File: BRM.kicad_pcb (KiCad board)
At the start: 4 copper layers, 48 parts, among them J1 2606-1102, J2 2601-1108, J4 2601-1108, U1 TPS55289RYQR

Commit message: VRM work
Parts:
- moved R1 123.5 mm to (98.2, 65.5), turned to 180 degrees
- moved D1 118.1 mm to (99.5, 67.5)
- moved D10 60.2 mm to (163.9, 133.6)
- moved Cvcc1 52.5 mm to (151.2, 45.0)
- moved Rt1 48.5 mm to (143.0, 43.5), turned to 90 degrees
- moved Coutx2 44.5 mm to (143.5, 54.0), turned to 180 degrees
- moved Coutx1 39.3 mm to (140.5, 59.0), turned to 180 degrees
- moved Rcomp1 35.1 mm to (147.8, 50.1), turned to 90 degrees
- moved J2 24.0 mm to (155.0, 75.5)
- moved L1 23.3 mm to (140.0, 68.5)
- moved Ccomp2 21.1 mm to (147.4, 52.5)
- moved Ccomp1 20.1 mm to (147.4, 51.5)
- moved F5 19.6 mm to (155.0, 57.4)
- moved Cboot1 19.4 mm to (138.0, 56.0)
- moved F6 18.9 mm to (162.0, 49.3)
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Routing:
- net Net-(U1-SW1): track 0.00 -> 73.2 mm
- net Net-(U1-SW2): track 0.00 -> 52.9 mm
- net /VRM/Vout: track 0.00 -> 29.8 mm, vias 0 -> 8
- net Net-(D5-A): track 87.1 -> 58.1 mm
- net Net-(D3-A): track 89.2 -> 60.2 mm
- net Net-(D9-A): track 0.00 -> 29.0 mm
- net Net-(D7-A): track 0.00 -> 29.0 mm
- net Net-(D8-A): track 0.00 -> 20.9 mm
- net Net-(D2-A): track 62.6 -> 41.7 mm
- net Net-(D4-A): track 62.6 -> 41.7 mm
- net Net-(D6-A): track 0.00 -> 20.9 mm
- net Net-(U1-BOOT1): track 0.00 -> 20.1 mm, vias 0 -> 2
- net Net-(U1-BOOT2): track 0.00 -> 19.8 mm
- net Net-(U1-EXTVCC): track 0.00 -> 9.89 mm, vias 0 -> 3
- net GND: track 6.50 -> 15.8 mm, vias 8 -> 87
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- added copper zone on F.Cu, net /VRM/Vout
- added copper zone on F.Cu, net GND
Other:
- copper layers 4 -> 2

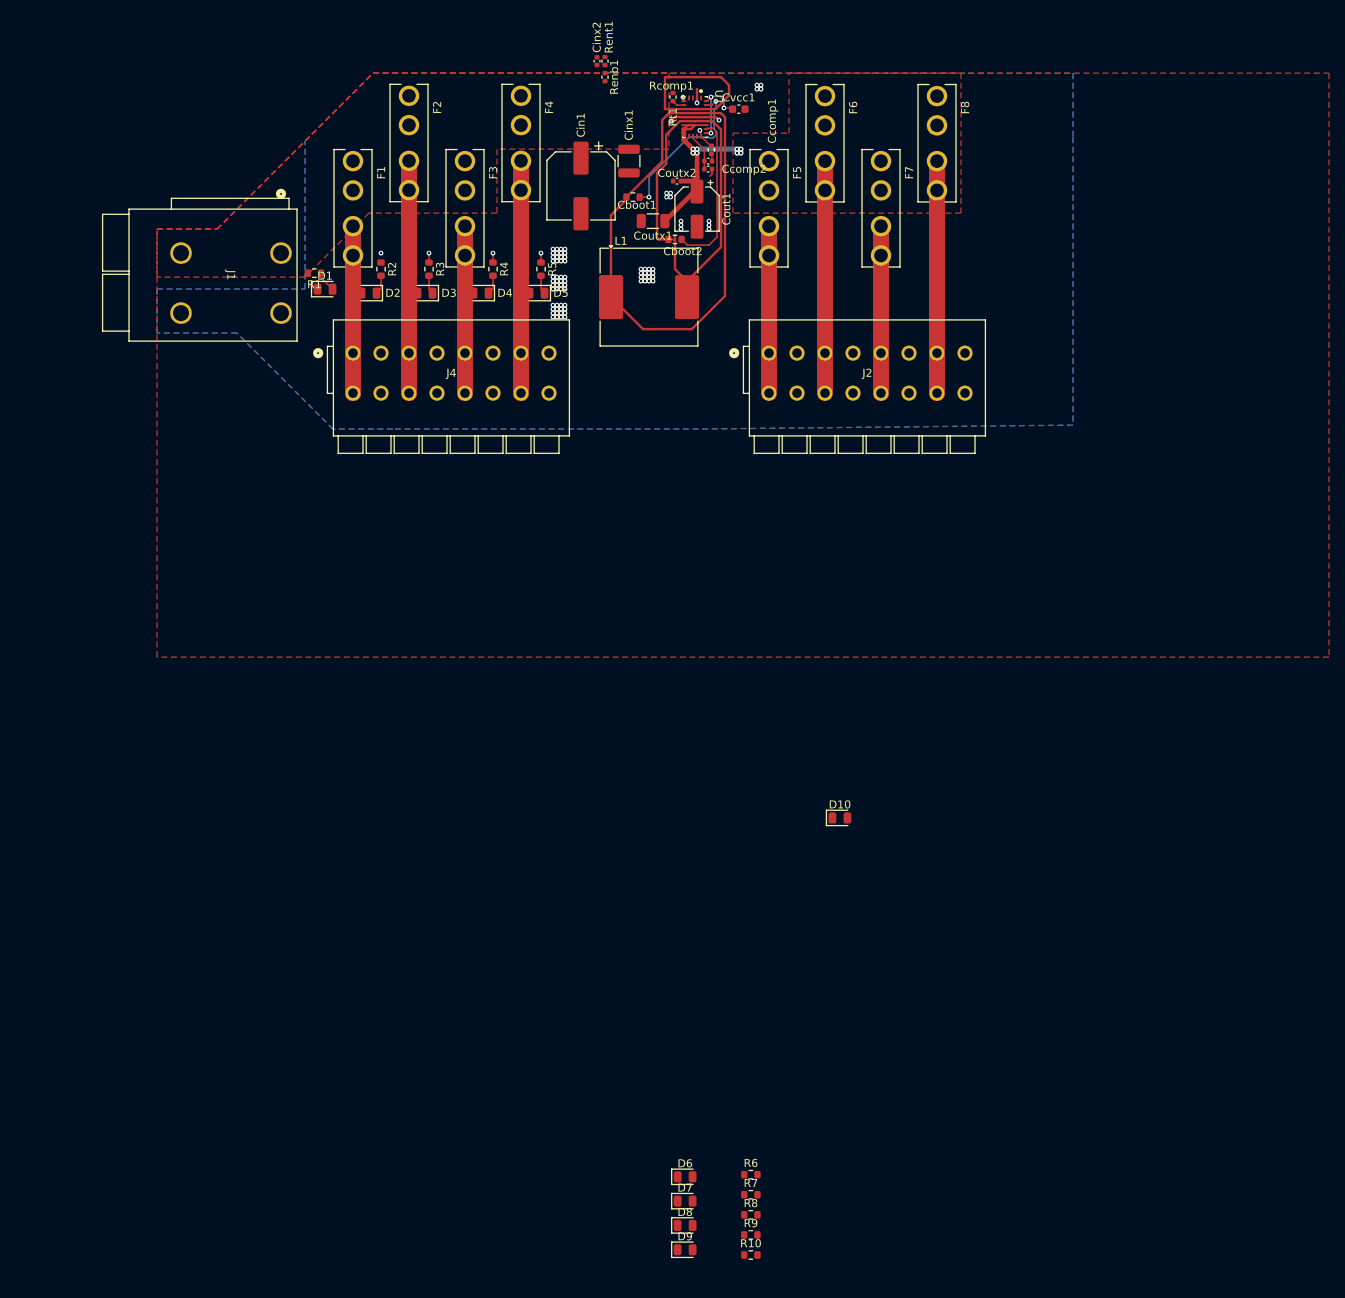
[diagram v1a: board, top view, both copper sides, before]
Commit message: DRC fixes and routing improvements
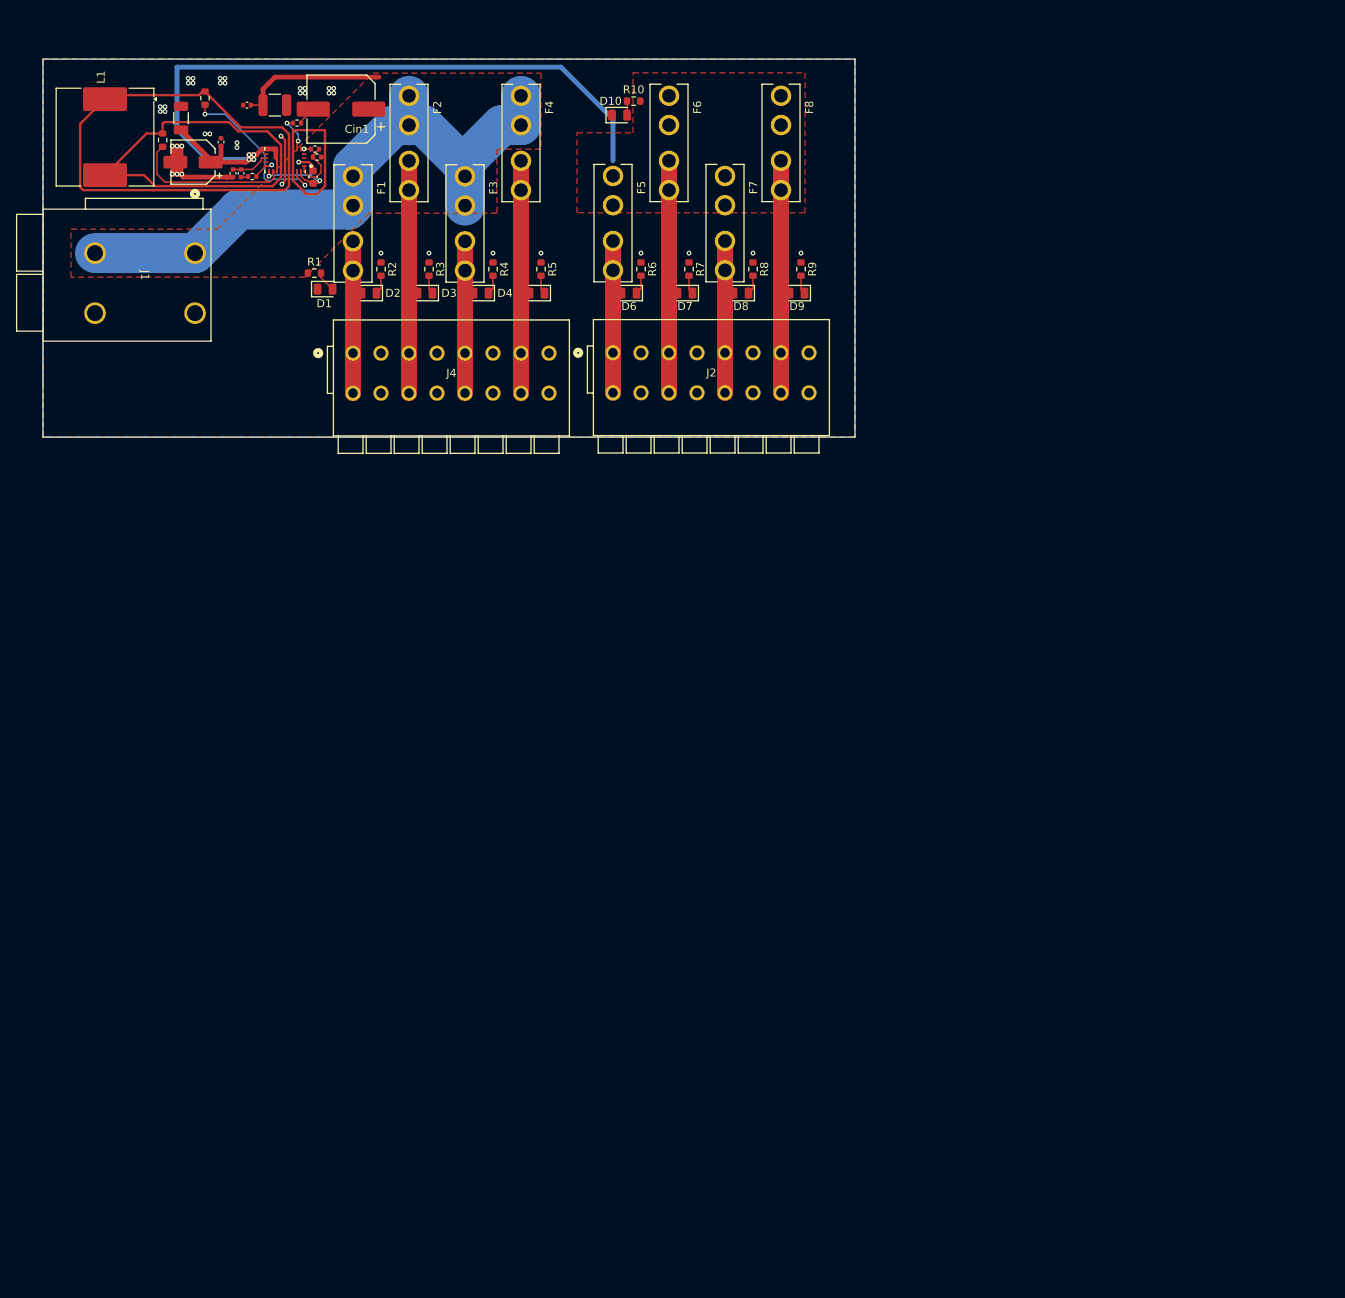
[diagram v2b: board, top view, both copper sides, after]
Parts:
- moved R10 145.0 mm to (138.1, 44.0)
- moved R9 120.9 mm to (159.0, 65.0), turned to -90 degrees
- moved D9 120.4 mm to (158.5, 68.0), turned to 180 degrees
- moved R8 118.2 mm to (153.0, 65.0), turned to -90 degrees
- moved D8 116.7 mm to (151.5, 68.0), turned to 180 degrees
- moved R7 116.0 mm to (145.0, 65.0), turned to -90 degrees
- moved R6 114.0 mm to (139.0, 65.0), turned to -90 degrees
- moved D7 113.5 mm to (144.5, 68.0), turned to 180 degrees
- moved D6 110.7 mm to (137.5, 68.0), turned to 180 degrees
- moved D10 92.1 mm to (136.3, 45.8)
- moved L1 70.9 mm to (72.0, 48.5), turned to -90 degrees
- moved Cboot2 65.2 mm to (79.2, 48.9), turned to -90 degrees
- moved Cout1 63.3 mm to (83.0, 51.6), turned to 180 degrees
- moved Coutx1 60.4 mm to (81.5, 46.1), turned to 90 degrees
- moved Ccomp2 59.4 mm to (88.0, 53.0), turned to -90 degrees
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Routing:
- net /12Vin: track 22.4 -> 122.3 mm
- net /VRM/Vout: track 29.8 -> 104.2 mm, vias 8 -> 4
- net Net-(D9-A): track 29.0 -> 58.0 mm
- net Net-(D7-A): track 29.0 -> 58.0 mm
- net GND: track 15.8 -> 36.6 mm, vias 87 -> 43
- net Net-(D8-A): track 20.9 -> 38.0 mm
- net Net-(D6-A): track 20.9 -> 37.9 mm
- net Net-(U1-EN_UVLO): track 0.00 -> 6.99 mm
- net Net-(D2-A): track 41.7 -> 38.0 mm
- net Net-(D4-A): track 41.7 -> 38.0 mm
- net Net-(U1-FSW): track 1.56 -> 4.61 mm, vias 0 -> 2
- net Net-(D8-K): track 0.00 -> 2.41 mm
- net Net-(D6-K): track 0.00 -> 2.41 mm
- net Net-(D9-K): track 0.00 -> 2.36 mm
- net Net-(D7-K): track 0.00 -> 2.36 mm
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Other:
- board outline added: 101.5 x 47.2 mm
